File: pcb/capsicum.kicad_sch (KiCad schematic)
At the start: 68 parts, among them J2 Screw_Terminal_01x02, J3 USB-C 16+8 USB 2.0, Q1 NS2101P, Q2 BC817, SW1 SW_SPDT, SW3 SW_SPDT, U1 ESP32-C3-WROOM-02, U2 TQ33E-1, U3 AP2112K, U4 MCP73831

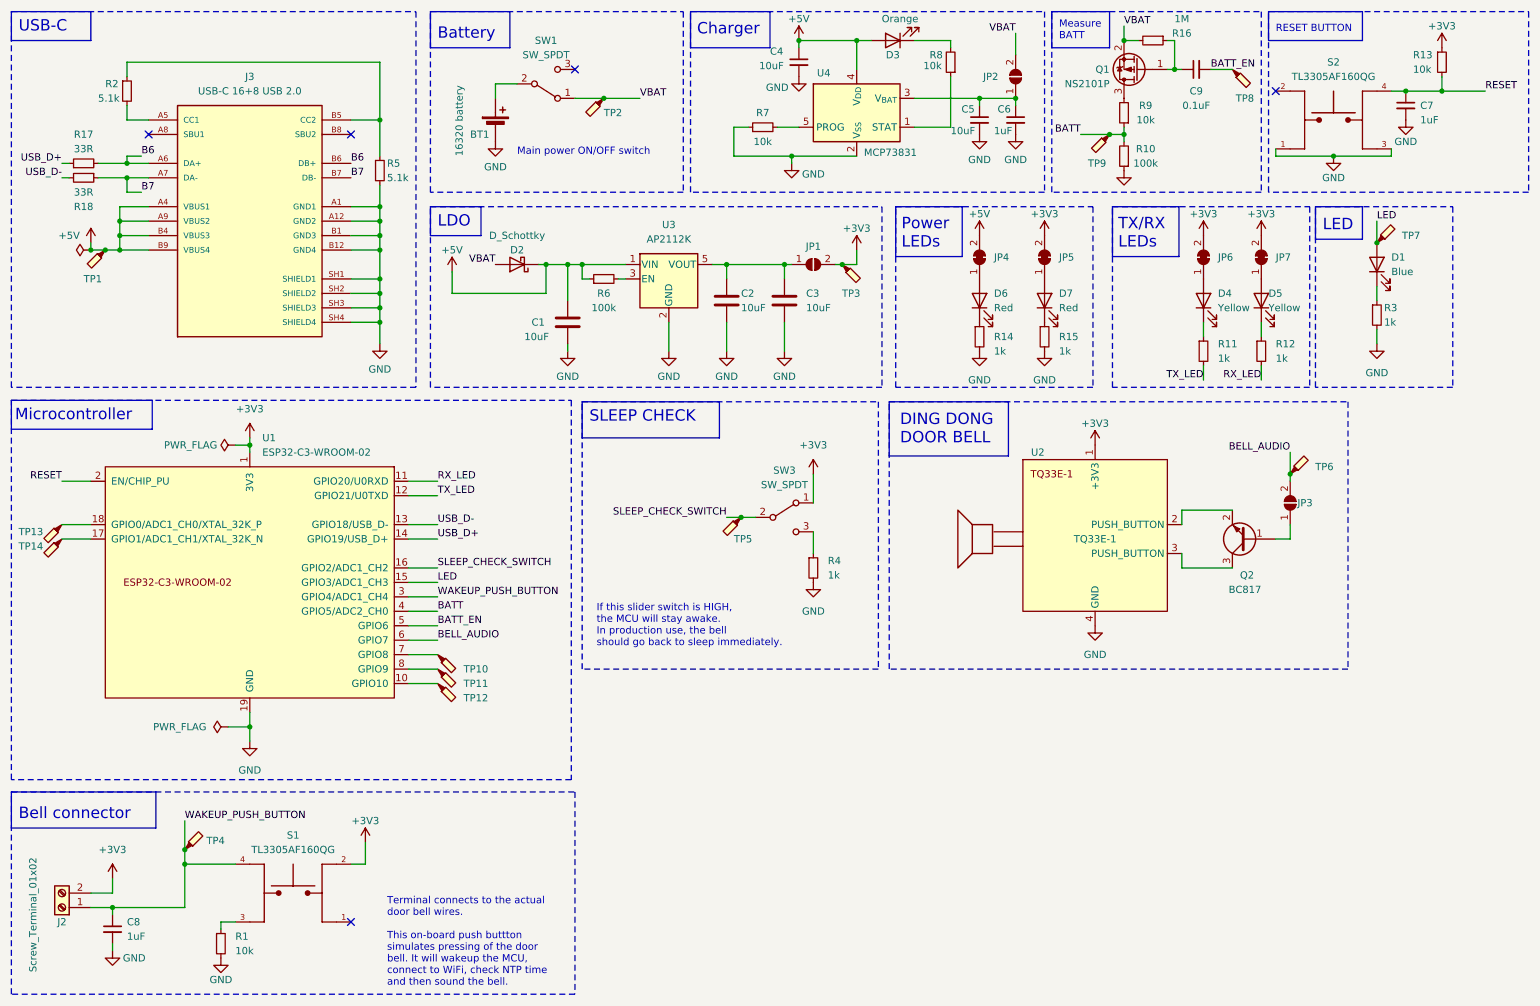
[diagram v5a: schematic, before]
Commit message: feat: publish bill of materials
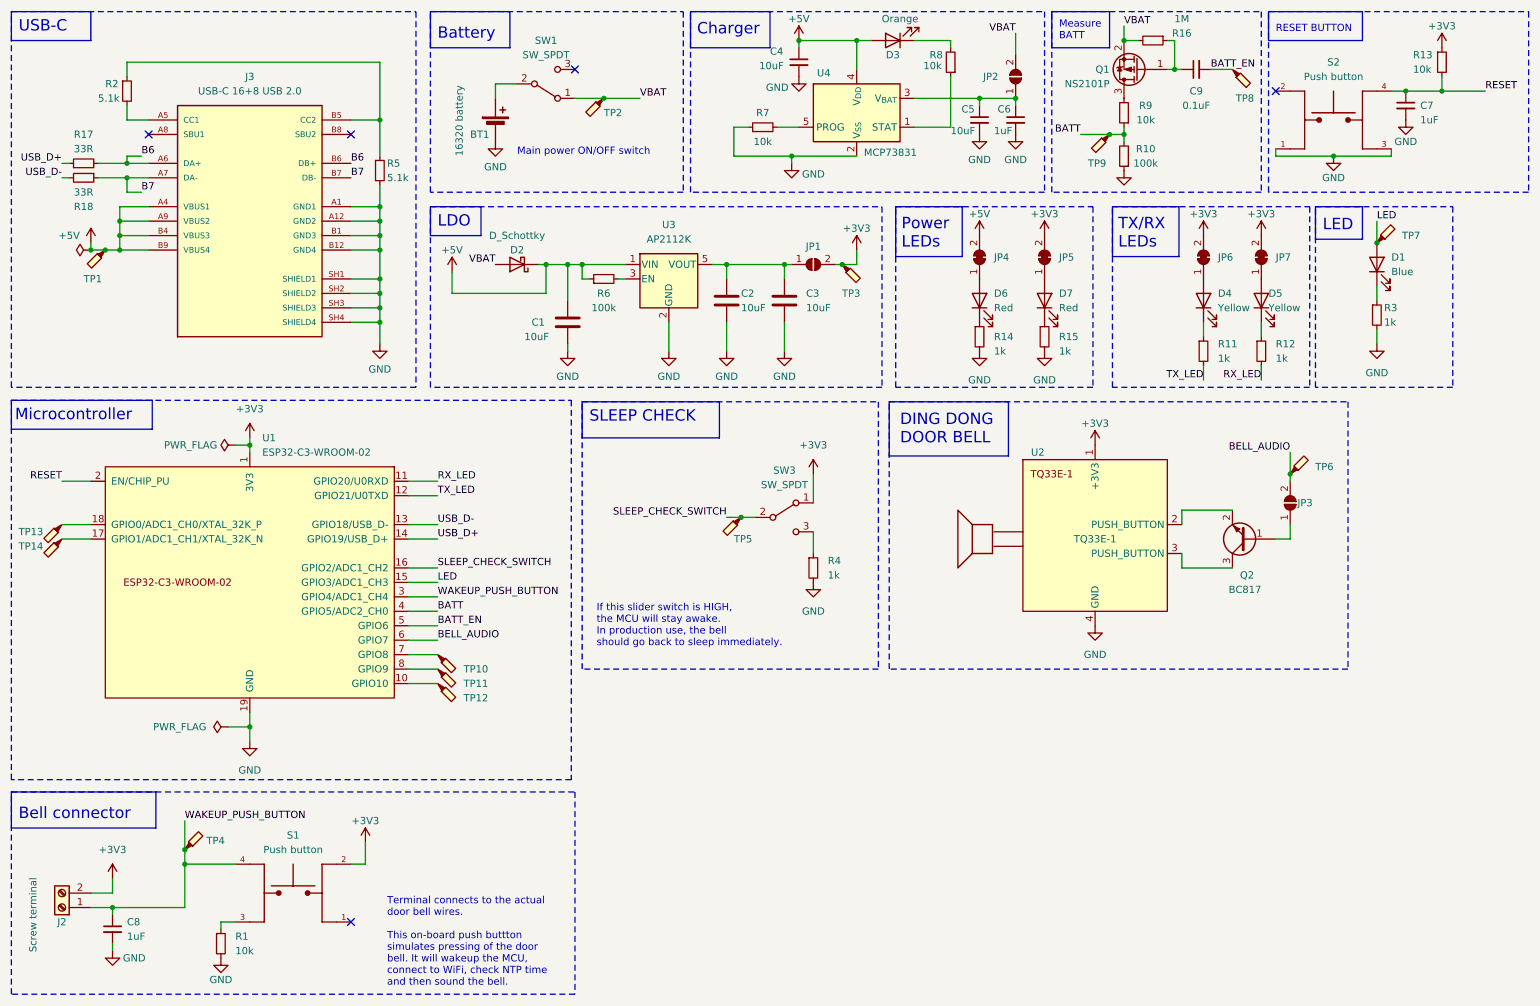
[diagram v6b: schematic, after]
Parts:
- BT1: Category (none) -> Connector; MANUFACTURER (none) -> EAEONXE; Package (none) -> SMD; Unit Price (USD) (none) -> 2.22
- C1, C2, C3, C4, C5: Category (none) -> Electronics; MANUFACTURER (none) -> YAGEO; Unit Price (USD) (none) -> 0.0284
- C6, C7, C8: Category (none) -> Electronics; MANUFACTURER (none) -> Kyocera; Unit Price (USD) (none) -> 0.1748
- C9: Category (none) -> Electronics; MANUFACTURER (none) -> Kyocera; Unit Price (USD) (none) -> 0.1028
- D1: Category (none) -> Electronics; Unit Price (USD) (none) -> 0.197
- D2: Category (none) -> Electronics; Unit Price (USD) (none) -> 0.5566
- D3: Category (none) -> Electronics; Unit Price (USD) (none) -> 0.1199
- D4, D5, D6, D7: Category (none) -> Electronics; Unit Price (USD) (none) -> 0.179
- J2: value Screw_Terminal_01x02 -> Screw terminal; Category (none) -> Connector; Unit Price (USD) (none) -> 0.2835
- J3: Category (none) -> Connector; Unit Price (USD) (none) -> 0.9651
- JP1, JP2, JP3: Category (none) -> Electronics; DNP (none) -> JP1, JP2, JP3; Unit Price (USD) (none) -> 0
- JP4, JP5, JP6, JP7: Category (none) -> Electronics; DNP (none) -> JP4, JP5, JP6, JP7; Unit Price (USD) (none) -> 0
- Q1: Category (none) -> Electronics; Unit Price (USD) (none) -> 0.4712
- Q2: Category (none) -> Electronics; Unit Price (USD) (none) -> 0.1593
- R1, R13, R7, R8, R9: Category (none) -> Electronics; Unit Price (USD) (none) -> 0.0038
- R10, R11, R12, R14, R15, R2, R3, R4, R5, R6: Category (none) -> Electronics; Unit Price (USD) (none) -> 0.1149
- R16: Category (none) -> Electronics; Unit Price (USD) (none) -> 0.0013
- R17, R18: Category (none) -> Electronics; Unit Price (USD) (none) -> 0.0208
- S1, S2: value TL3305AF160QG -> Push button; Category (none) -> Connector; Unit Price (USD) (none) -> 0.1701
- SW1: Category (none) -> Electronics; MANUFACTURER (none) -> NIDEC COPAL ELECTRONICS; Unit Price (USD) (none) -> 0.8033
- SW3: Category (none) -> Electronics; MANUFACTURER (none) -> NIDEC COPAL ELECTRONICS; Unit Price (USD) (none) -> 0.8033; Vendor (none) -> PCBWay
- TP1, TP10, TP11, TP12, TP13, TP14, TP2, TP3, TP4, TP5, TP6, TP7, TP8, TP9: Category (none) -> Electronics; DNP (none) -> TP1, TP2, TP3, TP4, TP5, TP6, TP7, TP8, TP9, TP10, TP11, TP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; Unit Price (USD) (none) -> 0
- U1: Category (none) -> Electronics; MANUFACTURER (none) -> Espressif; Unit Price (USD) (none) -> 2.6334
- U2: Category (none) -> Electronics; MANUFACTURER (none) -> FUERS; Unit Price (USD) (none) -> 3.22
- U3: Category (none) -> Electronics; MANUFACTURER (none) -> Diodes Incorporated; Unit Price (USD) (none) -> 0.1985
- U4: Category (none) -> Electronics; MANUFACTURER (none) -> Microchip; Unit Price (USD) (none) -> 0.8701

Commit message: feat: add right-angled header pin connector for the bell
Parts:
- U2: footprint Connector_PinHeader_2.54mm:PinHeader_1x04_P2.54mm_Vertical -> Connector_PinHeader_2.54mm:PinHeader_1x04_P2.54mm_Horizontal
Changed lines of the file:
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@@
       (effects (font (size 1.27 1.27)))
     )
-    (property "Footprint" "Connector_PinHeader_2.54mm:PinHeader_1x04_P2.54mm_Vertical" (at 207.01 110.49 0)
+    (property "Footprint" "Connector_PinHeader_2.54mm:PinHeader_1x04_P2.54mm_Horizontal" (at 207.01 110.49 0)
       (effects (font (size 1.27 1.27)) hide)
     )

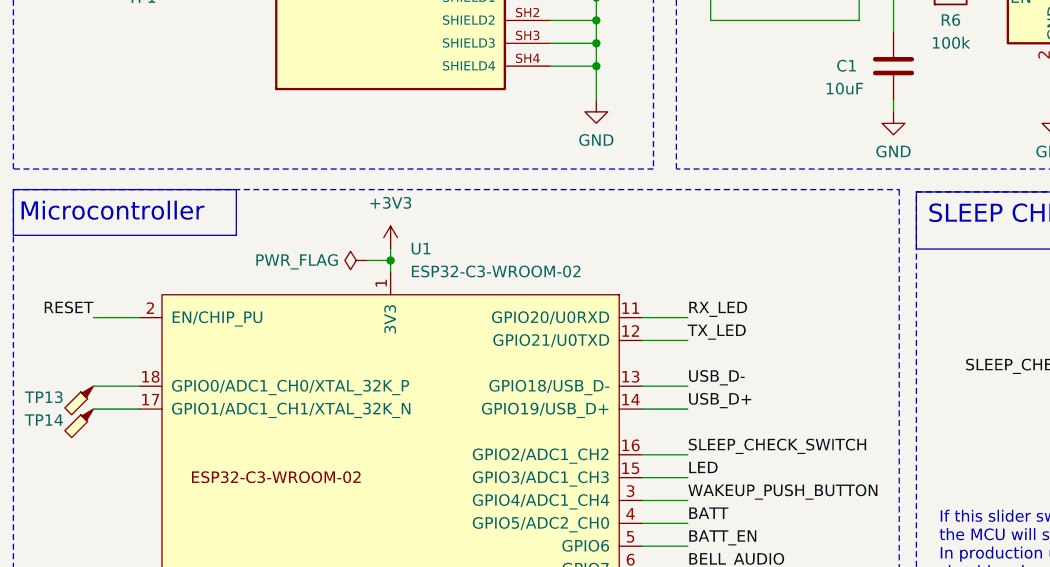
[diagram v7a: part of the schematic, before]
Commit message: feat: add 2 capacitors to 3.3V of the MCU
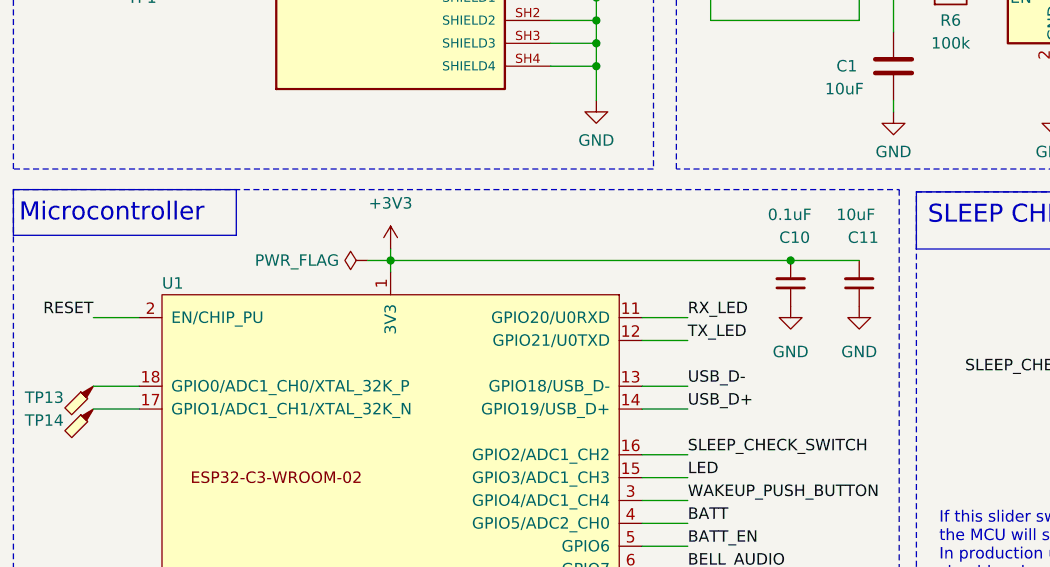
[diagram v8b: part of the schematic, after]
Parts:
- added C10: 0.1uF, Capacitor_SMD:C_0603_1608Metric, symbol Device:C_Small
- added C11: 10uF, Capacitor_SMD:C_0603_1608Metric, symbol Device:C_Small
- D1: Vendor PCBWAY -> PCBWay
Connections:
- net +3V3: now also C10.2, C11.2
- net GND: now also C10.1, C11.1
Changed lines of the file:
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@@
   (junction (at 165.1 22.86) (diameter 0) (color 0 0 0 0)
   )
+  (junction (at 102.87 93.98) (diameter 0) (color 0 0 0 0)
+  )
   (junction (at 58.42 143.51) (diameter 0) (color 0 0 0 0)
   )
@@
     (stroke (width 0) (type default))
   )
+  (wire (pts (xy 102.87 93.98) (xy 110.49 93.98))
+    (stroke (width 0) (type default))
+  )
   (wire (pts (xy 222.25 113.03) (xy 222.25 115.57))
     (stroke (width 0) (type default))
@@
     (stroke (width 0) (type default))
   )
+  (wire (pts (xy 58.42 93.98) (xy 102.87 93.98))
+    (stroke (width 0) (type default))
+  )
   (wire (pts (xy 39.37 49.53) (xy 36.83 49.53))
     (stroke (width 0) (type default))
@@
     )
   )
+  (symbol (lib_id "power:GND") (at 110.49 99.06 0) (unit 1)
+    (in_bom yes) (on_board yes) (dnp no) (fields_autoplaced)
+    (property "Reference" "#PWR035" (at 110.49 105.41 0)
+      (effects (font (size 1.27 1.27)) hide)
+    )
+    (property "Value" "GND" (at 110.49 104.14 0)
+      (effects (font (size 1.27 1.27)))
+    )
+    (property "Footprint" "" (at 110.49 99.06 0)
+      (effects (font (size 1.27 1.27)) hide)
+    )
+    (property "Datasheet" "" (at 110.49 99.06 0)
+      (effects (font (size 1.27 1.27)) hide)
+    )
+    (pin "1")
+    (instances
+      (project "capsicum"
+        (path "/b2b89cea-f415-45cb-9116-7d102948da73"
+          (reference "#PWR035") (unit 1)
+        )
+      )
+    )
+  )
   (symbol (lib_id "Switch:SW_SPDT") (at 110.49 30.48 0) (mirror x) (unit 1)
     (in_bom yes) (on_board yes) (dnp no)
@@
       (effects (font (size 1.27 1.27)) hide)
     )
-    (property "Vendor" "PCBWAY" (at 256.54 62.23 0)
+    (property "Vendor" "PCBWay" (at 256.54 62.23 0)
       (effects (font (size 1.27 1.27)) hide)
     )
@@
     )
   )
+  (symbol (lib_id "Device:C_Small") (at 110.49 96.52 180) (unit 1)
+    (in_bom yes) (on_board yes) (dnp no)
+    (property "Reference" "C11" (at 109.22 91.44 0)
+      (effects (font (size 1.27 1.27)) (justify right))
+    )
+    (property "Value" "10uF" (at 107.95 88.9 0)
+      (effects (font (size 1.27 1.27)) (justify right))
+    )
+    (property "Footprint" "Capacitor_SMD:C_0603_1608Metric" (at 110.49 96.52 0)
+      (effects (font (size 1.27 1.27)) hide)
+    )
+    (property "Datasheet" "https://www.yageo.com/upload/website/yageo_High%20Capacitance%20MLCCs_2016_19050911_141.pdf" (at 110.49 96.52 0)
+      (effects (font (size 1.27 1.27)) hide)
+    )
+    (property "Category" "Electronics" (at 110.49 96.52 0)
+      (effects (font (size 1.27 1.27)) hide)
+    )
+    (property "Link" "https://www.pcbway.com/components/detail/CC0603KRX5R6BB106/1422744/" (at 110.49 96.52 0)
+      (effects (font (size 1.27 1.27)) hide)
+    )
+    (property "MANUFACTURER" "YAGEO" (at 110.49 96.52 0)
+      (effects (font (size 1.27 1.27)) hide)
+    )
+    (property "MPN" "CC0603KRX5R6BB106" (at 110.49 96.52 0)
+      (effects (font (size 1.27 1.27)) hide)
+    )
+    (property "Package" "0603" (at 110.49 96.52 0)
+      (effects (font (size 1.27 1.27)) hide)
+    )
+    (property "Unit Price (USD)" "0.0284" (at 110.49 96.52 0)
+      (effects (font (size 1.27 1.27)) hide)
+    )
+    (property "Vendor" "PCBWay" (at 110.49 96.52 0)
+      (effects (font (size 1.27 1.27)) hide)
+    )
+    (pin "1")
+    (pin "2")
+    (instances
+      (project "capsicum"
+        (path "/b2b89cea-f415-45cb-9116-7d102948da73"
+          (reference "C11") (unit 1)
+        )
+      )
+    )
+  )
   (symbol (lib_id "Connector:TestPoint_Probe") (at 144.78 106.68 180) (unit 1)
     (in_bom yes) (on_board yes) (dnp no)
@@
     )
   )
+  (symbol (lib_id "Device:C_Small") (at 102.87 96.52 180) (unit 1)
+    (in_bom yes) (on_board yes) (dnp no)
+    (property "Reference" "C10" (at 101.6 91.44 0)
+      (effects (font (size 1.27 1.27)) (justify right))
+    )
+    (property "Value" "0.1uF" (at 100.33 88.9 0)
+      (effects (font (size 1.27 1.27)) (justify right))
+    )
+    (property "Footprint" "Capacitor_SMD:C_0603_1608Metric" (at 102.87 96.52 0)
+      (effects (font (size 1.27 1.27)) hide)
+    )
+    (property "Datasheet" "https://datasheets.kyocera-avx.com/X7RDielectric.pdf" (at 102.87 96.52 0)
+      (effects (font (size 1.27 1.27)) hide)
+    )
+    (property "Category" "Electronics" (at 102.87 96.52 0)
+      (effects (font (size 1.27 1.27)) hide)
+    )
+    (property "Link" "https://www.pcbway.com/components/detail/06033C104KAT4A/92726/" (at 102.87 96.52 0)
+      (effects (font (size 1.27 1.27)) hide)
+    )
+    (property "MANUFACTURER" "Kyocera" (at 102.87 96.52 0)
+      (effects (font (size 1.27 1.27)) hide)
+    )
+    (property "MPN" "06033C104KAT4A" (at 102.87 96.52 0)
+      (effects (font (size 1.27 1.27)) hide)
+    )
+    (property "Package" "0603" (at 102.87 96.52 0)
+      (effects (font (size 1.27 1.27)) hide)
+    )
+    (property "Unit Price (USD)" "0.1028" (at 102.87 96.52 0)
+      (effects (font (size 1.27 1.27)) hide)
+    )
+    (property "Vendor" "PCBWay" (at 102.87 96.52 0)
+      (effects (font (size 1.27 1.27)) hide)
+    )
+    (pin "1")
+    (pin "2")
+    (instances
+      (project "capsicum"
+        (path "/b2b89cea-f415-45cb-9116-7d102948da73"
+          (reference "C10") (unit 1)
+        )
+      )
+    )
+  )
   (symbol (lib_id "Device:LED") (at 198.12 68.58 90) (unit 1)
     (in_bom yes) (on_board yes) (dnp no)
@@
   )
   (symbol (lib_id "Espressif:ESP32-C3-WROOM-02") (at 58.42 118.11 0) (unit 1)
-    (in_bom yes) (on_board yes) (dnp no) (fields_autoplaced)
-    (property "Reference" "U1" (at 60.6141 92.71 0)
+    (in_bom yes) (on_board yes) (dnp no)
+    (property "Reference" "U1" (at 33.02 96.52 0)
       (effects (font (size 1.27 1.27)) (justify left))
     )
     (property "Value" "ESP32-C3-WROOM-02" (at 60.6141 95.25 0)
-      (effects (font (size 1.27 1.27)) (justify left))
+      (effects (font (size 1.27 1.27)) (justify left) hide)
     )
     (property "Footprint" "Espressif:ESP32-C3-WROOM-02" (at 58.42 148.59 0)
@@
         )
       )
+    )
+  )
+  (symbol (lib_id "power:GND") (at 102.87 99.06 0) (unit 1)
+    (in_bom yes) (on_board yes) (dnp no) (fields_autoplaced)
+    (property "Reference" "#PWR013" (at 102.87 105.41 0)
+      (effects (font (size 1.27 1.27)) hide)
+    )
+    (property "Value" "GND" (at 102.87 104.14 0)
+      (effects (font (size 1.27 1.27)))
+    )
+    (property "Footprint" "" (at 102.87 99.06 0)
+      (effects (font (size 1.27 1.27)) hide)
+    )
+    (property "Datasheet" "" (at 102.87 99.06 0)
+      (effects (font (size 1.27 1.27)) hide)
+    )
+    (pin "1")
+    (instances
+      (project "capsicum"
+        (path "/b2b89cea-f415-45cb-9116-7d102948da73"
+          (reference "#PWR013") (unit 1)
+        )
+      )
